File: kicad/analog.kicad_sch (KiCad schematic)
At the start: 25 parts, among them U5 74HC4051, U6 74HC4051, U7 OPA350

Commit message: completed matrix
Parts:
- U5, U6: footprint cipulot_parts:TSSOP16 -> footprints:TSSOP16
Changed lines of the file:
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@@
 			)
 		)
-		(property "Footprint" "cipulot_parts:TSSOP16"
+		(property "Footprint" "footprints:TSSOP16"
 			(at 127 95.25 0)
 			(effects
@@
 			)
 		)
-		(property "Footprint" "cipulot_parts:TSSOP16"
+		(property "Footprint" "footprints:TSSOP16"
 			(at 149.86 135.89 0)
 			(effects

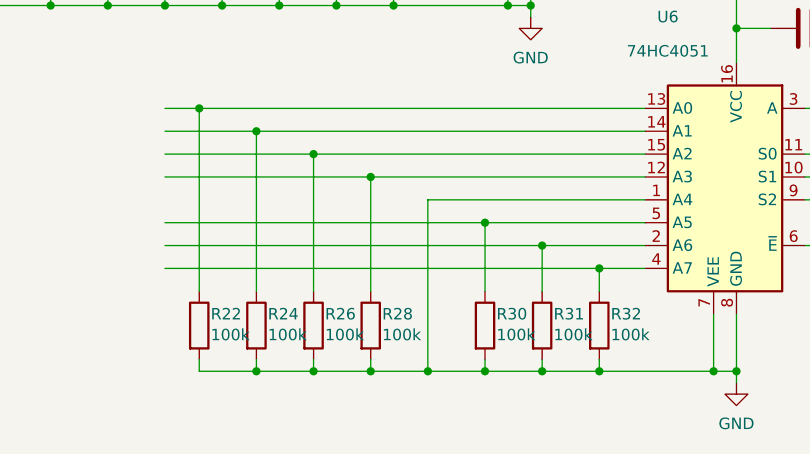
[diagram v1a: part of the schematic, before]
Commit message: replaced half of the matrix
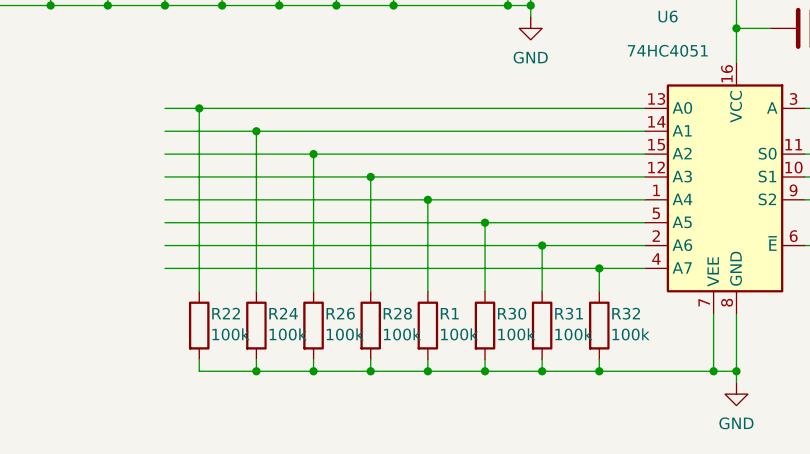
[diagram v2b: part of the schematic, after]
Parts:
- added R1: 100k, Resistor_SMD:R_0402_1005Metric, symbol Device:R
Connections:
- net GND: now also R1.2; no longer U6.1 (A4)
- new net: R1.1, U6.1 (A4)
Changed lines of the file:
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@@
 	(paper "A4")
 	(junction
-		(at 115.57 147.32)
-		(diameter 0)
-		(color 0 0 0 0)
-	)
-	(junction
 		(at 128.27 133.35)
 		(diameter 0)
@@
 	)
 	(junction
+		(at 115.57 147.32)
+		(diameter 0)
+		(color 0 0 0 0)
+	)
+	(junction
 		(at 121.92 130.81)
 		(diameter 0)
@@
 	)
 	(junction
+		(at 115.57 128.27)
+		(diameter 0)
+		(color 0 0 0 0)
+	)
+	(junction
 		(at 248.92 86.36)
 		(diameter 0)
@@
 	(wire
 		(pts
+			(xy 86.36 128.27) (xy 115.57 128.27)
+		)
+		(stroke
+			(width 0)
+			(type default)
+		)
+	)
+	(wire
+		(pts
 			(xy 220.98 97.79) (xy 227.965 97.79)
 		)
@@
 	(wire
 		(pts
-			(xy 139.7 128.27) (xy 115.57 128.27)
+			(xy 147.32 147.32) (xy 149.86 147.32)
 		)
 		(stroke
@@
 	(wire
 		(pts
-			(xy 147.32 147.32) (xy 149.86 147.32)
+			(xy 246.38 90.17) (xy 246.38 102.87)
 		)
 		(stroke
@@
 	(wire
 		(pts
-			(xy 246.38 90.17) (xy 246.38 102.87)
+			(xy 109.22 146.05) (xy 109.22 147.32)
 		)
 		(stroke
@@
 	(wire
 		(pts
-			(xy 109.22 146.05) (xy 109.22 147.32)
+			(xy 115.57 128.27) (xy 115.57 138.43)
 		)
 		(stroke
@@
 	(wire
 		(pts
+			(xy 115.57 147.32) (xy 121.92 147.32)
+		)
+		(stroke
+			(width 0)
+			(type default)
+		)
+	)
+	(wire
+		(pts
 			(xy 239.395 109.22) (xy 240.665 109.22)
 		)
@@
 	(wire
 		(pts
-			(xy 138.43 68.58) (xy 140.97 68.58)
+			(xy 115.57 128.27) (xy 139.7 128.27)
 		)
 		(stroke
@@
 	(wire
 		(pts
-			(xy 99.06 90.17) (xy 63.5 90.17)
+			(xy 138.43 68.58) (xy 140.97 68.58)
 		)
 		(stroke
@@
 	(wire
 		(pts
-			(xy 121.92 130.81) (xy 86.36 130.81)
+			(xy 99.06 90.17) (xy 63.5 90.17)
 		)
 		(stroke
@@
 	(wire
 		(pts
-			(xy 203.2 83.82) (xy 220.98 83.82)
+			(xy 121.92 130.81) (xy 86.36 130.81)
 		)
 		(stroke
@@
 	(wire
 		(pts
-			(xy 115.57 147.32) (xy 121.92 147.32)
+			(xy 203.2 83.82) (xy 220.98 83.82)
 		)
 		(stroke
@@
 	(wire
 		(pts
-			(xy 115.57 128.27) (xy 115.57 147.32)
+			(xy 73.66 105.41) (xy 73.66 106.68)
 		)
 		(stroke
@@
 	(wire
 		(pts
-			(xy 73.66 105.41) (xy 73.66 106.68)
+			(xy 111.76 105.41) (xy 111.76 106.68)
 		)
 		(stroke
@@
 	(wire
 		(pts
-			(xy 111.76 105.41) (xy 111.76 106.68)
+			(xy 105.41 97.79) (xy 105.41 92.71)
 		)
 		(stroke
@@
 	(wire
 		(pts
-			(xy 105.41 97.79) (xy 105.41 92.71)
+			(xy 86.36 106.68) (xy 92.71 106.68)
 		)
 		(stroke
@@
 	(wire
 		(pts
-			(xy 86.36 106.68) (xy 92.71 106.68)
+			(xy 92.71 105.41) (xy 92.71 106.68)
 		)
 		(stroke
@@
 	(wire
 		(pts
-			(xy 92.71 105.41) (xy 92.71 106.68)
+			(xy 115.57 146.05) (xy 115.57 147.32)
 		)
 		(stroke
@@
 					(unit 1)
 				)
+			)
+		)
+	)
+	(symbol
+		(lib_id "Device:R")
+		(at 115.57 142.24 0)
+		(unit 1)
+		(exclude_from_sim no)
+		(in_bom yes)
+		(on_board yes)
+		(dnp no)
+		(property "Reference" "R1"
+			(at 116.84 140.97 0)
+			(effects
+				(font
+					(size 1.27 1.27)
+				)
+				(justify left)
+			)
+		)
+		(property "Value" "100k"
+			(at 116.84 143.2814 0)
+			(effects
+				(font
+					(size 1.27 1.27)
+				)
+				(justify left)
+			)
+		)
+		(property "Footprint" "Resistor_SMD:R_0402_1005Metric"
+			(at 113.792 142.24 90)
+			(effects
+				(font
+					(size 1.27 1.27)
+				)
+				(hide yes)
+			)
+		)
+		(property "Datasheet" "~"
+			(at 115.57 142.24 0)
+			(effects
+				(font
+					(size 1.27 1.27)
+				)
+				(hide yes)
+			)
+		)
+		(property "Description" ""
+			(at 115.57 142.24 0)
+			(effects
+				(font
+					(size 1.27 1.27)
+				)
+				(hide yes)
+			)
+		)
+		(property "LCSC" "C25741"
+			(at 115.57 142.24 0)
+			(effects
+				(font
+					(size 1.27 1.27)
+				)
+				(hide yes)
+			)
+		)
+		(pin "1"
+		)
+		(pin "2"
+		)
+		(instances
+			(project "toprebox_prototype"
+				(path "/8da5c518-ba63-450e-856e-258a7a1195e6/1693d11f-4de1-427b-b922-4b4751bb19d2"
+					(reference "R1")
+					(unit 1)
+				)

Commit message: matrix complete
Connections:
- net C5: now reaches R25.1, U5.5 (A5)
- net C7: now reaches R31.1, U6.2 (A6)
- net C4: now reaches R23.1, U5.1 (A4)
- net C3: now reaches R21.1, U5.12 (A3)
- net C0: now reaches R18.1, U5.13 (A0)
- net C1: now reaches R19.1, U5.14 (A1)
- net C2: now reaches R20.1, U5.15 (A2)
- net C6: now reaches R1.1, U6.1 (A4)

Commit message: stuff
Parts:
- renumbered C5 to C1, C7 to C2, C8 to C3, C6 to C4, JP2 to JP1, R34 to R1, R33 to R10, R22 to R11, R24 to R12, R26 to R13, R28 to R14, R1 to R15, R30 to R16, R31 to R17, R32 to R18, R18 to R2, R19 to R3, R20 to R4, R21 to R5, R23 to R6, R25 to R7, R27 to R8, R29 to R9, U5 to U1, U7 to U3, U6 to U4
